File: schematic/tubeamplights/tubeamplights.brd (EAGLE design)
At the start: 68.8 x 53 mm, 6 parts

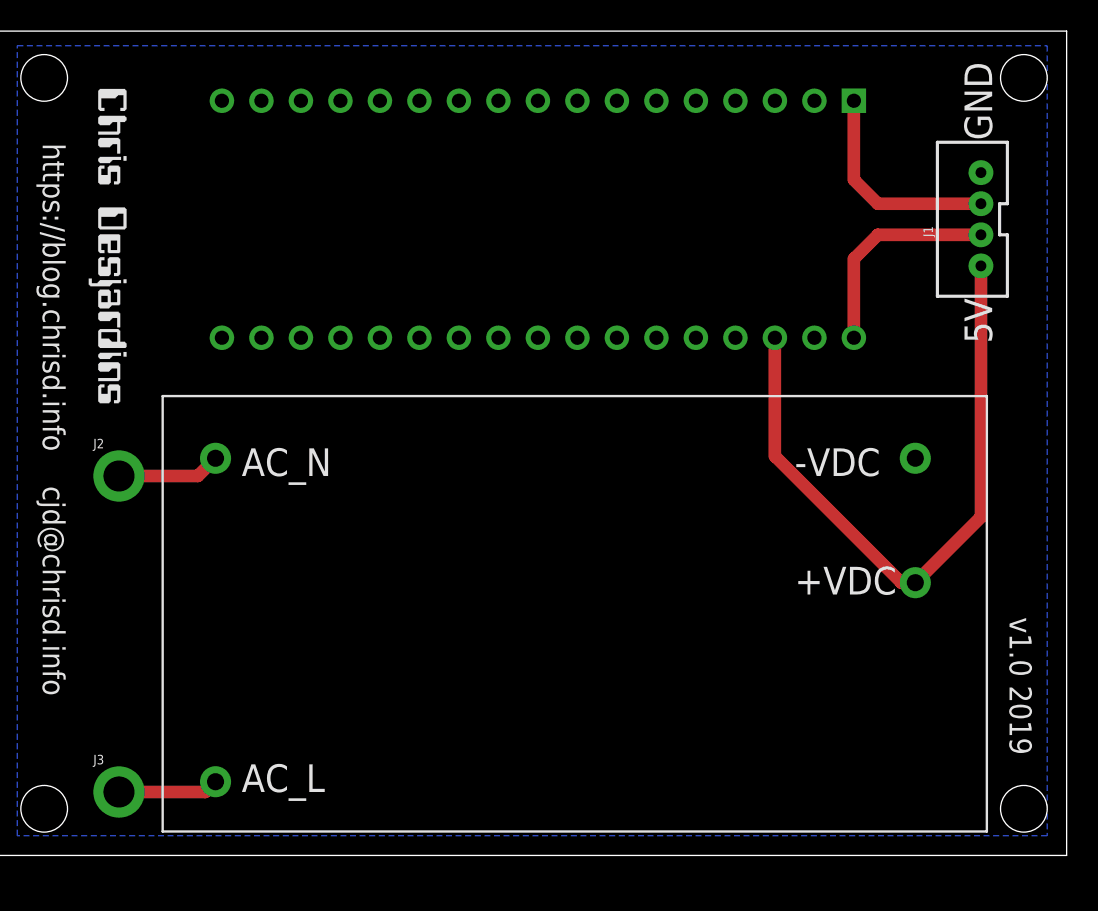
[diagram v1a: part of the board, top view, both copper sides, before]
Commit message: Fix the reg footprint
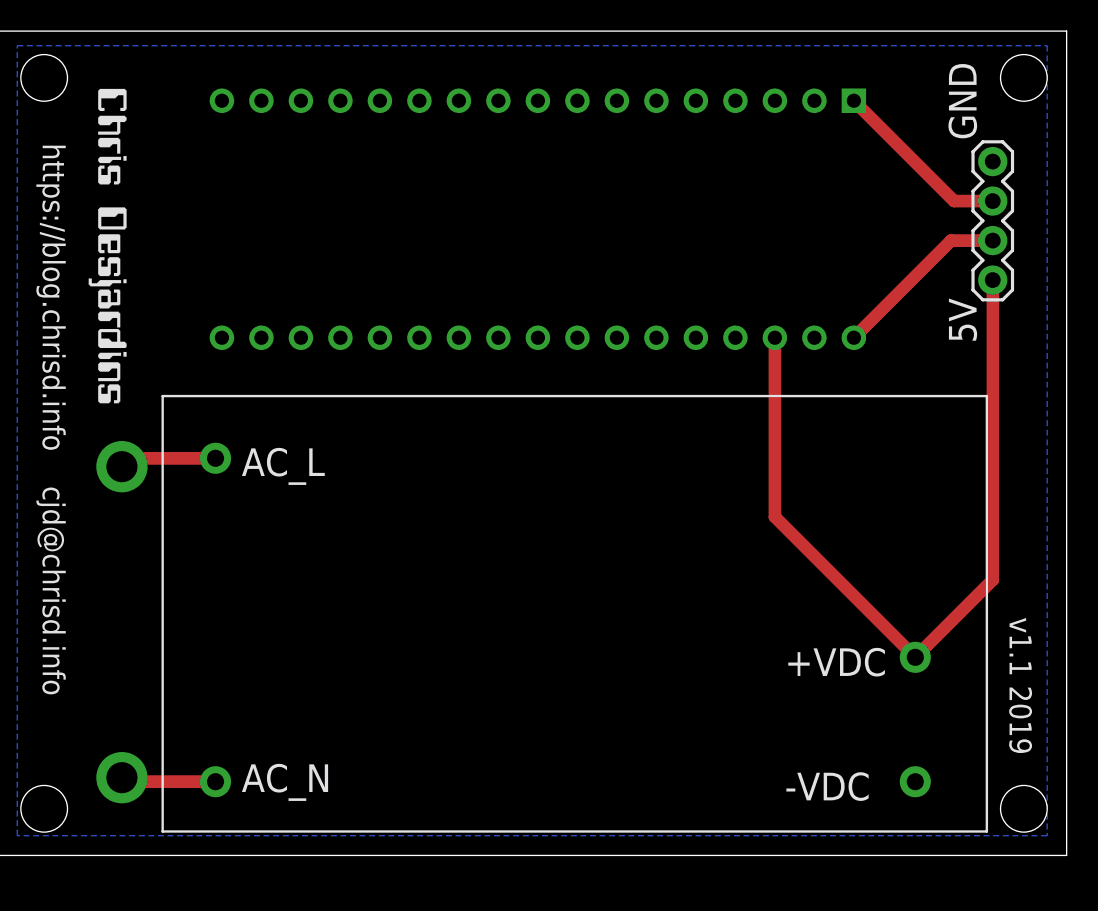
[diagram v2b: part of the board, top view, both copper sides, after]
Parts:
- removed J1: (no value), SparkFun-Connectors:JST-4-PTH-VERT
- added J4: (no value), SparkFun-Connectors:1X04
- moved J3 20.9 mm to (8.00, 25.0)
- moved J2 19.4 mm to (8.00, 5.00)
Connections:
- net GND: now also J4.4; no longer J1.4
- net MOSI: now also J4.3; no longer J1.3
- net SCK: now also J4.2; no longer J1.2
- net VIN: now also J4.1; no longer J1.1
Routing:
- net VIN: track 42.1 -> 50.6 mm
- net SCK: track 13.9 -> 11.5 mm
- net MOSI: track 13.9 -> 11.6 mm
- net AC_N: track 6.68 -> 6.13 mm
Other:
- board text added: "v1.1 2019"
- board text removed: "v1.0 2019"
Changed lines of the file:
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@@
 <wire x1="0" y1="53.01" x2="0" y2="0" width="0" layer="20"/>
 <text x="2.905" y="45.8" size="1.4224" layer="21" font="vector" rot="SR270">https://blog.chrisd.info    cjd@chrisd.info</text>
-<text x="63.96" y="35.83" size="1.778" layer="21" rot="R90" align="bottom-right">5V</text>
-<text x="63.96" y="45.99" size="1.778" layer="21" rot="R90">GND</text>
-<text x="65.08" y="15.32" size="1.4224" layer="21" font="vector" rot="SR270">v1.0 2019</text>
+<text x="62.96" y="35.83" size="1.778" layer="21" rot="R90" align="bottom-right">5V</text>
+<text x="62.96" y="45.99" size="1.778" layer="21" rot="R90">GND</text>
+<text x="65.08" y="15.32" size="1.4224" layer="21" font="vector" rot="SR270">v1.1 2019</text>
 <hole x="66" y="3" drill="3"/>
 <hole x="66" y="50" drill="3"/>
@@
 </autorouter>
 <elements>
-<element name="J1" library="SparkFun-Connectors" library_urn="urn:adsk.eagle:library:513" package="JST-4-PTH-VERT" package3d_urn="urn:adsk.eagle:package:38102/1" value="" x="62.69" y="40.91" smashed="yes" rot="R90">
-<attribute name="NAME" x="60.15" y="39.767" size="0.6096" layer="25" font="vector" ratio="20" rot="R90"/>
-<attribute name="PROD_ID" value="CONN-13251" x="143.97" y="58.69" size="1.778" layer="27" rot="R90" display="off"/>
-<attribute name="VALUE" x="65.992" y="39.259" size="0.6096" layer="27" font="vector" ratio="20" rot="R90"/>
+<element name="J2" library="SparkFun-Connectors" library_urn="urn:adsk.eagle:library:513" package="1X01_2MM" package3d_urn="urn:adsk.eagle:package:38029/1" value="" x="8" y="5" smashed="yes">
+<attribute name="VALUE" x="6.349" y="2.587" size="0.6096" layer="27" font="vector" ratio="20"/>
 </element>
-<element name="J2" library="SparkFun-Connectors" library_urn="urn:adsk.eagle:library:513" package="1X01_2MM" package3d_urn="urn:adsk.eagle:package:38029/1" value="" x="7.81" y="24.4" smashed="yes">
-<attribute name="NAME" x="6.159" y="26.178" size="0.6096" layer="25" font="vector" ratio="20"/>
-<attribute name="VALUE" x="6.159" y="21.987" size="0.6096" layer="27" font="vector" ratio="20"/>
-</element>
-<element name="J3" library="SparkFun-Connectors" library_urn="urn:adsk.eagle:library:513" package="1X01_2MM" package3d_urn="urn:adsk.eagle:package:38029/1" value="" x="7.81" y="4.08" smashed="yes">
-<attribute name="NAME" x="6.159" y="5.858" size="0.6096" layer="25" font="vector" ratio="20"/>
-<attribute name="VALUE" x="6.159" y="1.667" size="0.6096" layer="27" font="vector" ratio="20"/>
+<element name="J3" library="SparkFun-Connectors" library_urn="urn:adsk.eagle:library:513" package="1X01_2MM" package3d_urn="urn:adsk.eagle:package:38029/1" value="" x="8" y="25" smashed="yes">
+<attribute name="VALUE" x="6.349" y="22.587" size="0.6096" layer="27" font="vector" ratio="20"/>
 </element>
 <element name="U$1" library="ChrisD" package="ARDUINO_PRO_MICRO" value="ARDUINO_PRO_MICRO" x="10.62" y="49.8" smashed="yes" rot="R270"/>
 <element name="U$2" library="meanwell-mpm-20-x" package="MPM-20-X" value="MPM-20-X" x="10.62" y="1.54" smashed="yes"/>
 <element name="U$3" library="desjardins" package="LOGO" value="" x="6.4725" y="49.37" smashed="yes" rot="R270"/>
+<element name="J4" library="SparkFun-Connectors" library_urn="urn:adsk.eagle:library:513" package="1X04" package3d_urn="urn:adsk.eagle:package:38085/1" value="" x="64" y="37" smashed="yes" rot="R90">
+<attribute name="PROD_ID" value="CONN-09696" x="64" y="37" size="1.778" layer="27" rot="R90" display="off"/>
+<attribute name="VALUE" x="66.032" y="35.73" size="0.6096" layer="27" font="vector" ratio="20" rot="R90"/>
+</element>
 </elements>
 <signals>
@@
 <contactref element="U$2" pad="+VDC"/>
 <contactref element="U$1" pad="P32"/>
-<contactref element="J1" pad="1"/>
-<wire x1="59.02" y1="17.54" x2="58.12" y2="17.54" width="0.8128" layer="1"/>
-<wire x1="58.12" y1="17.54" x2="49.99" y2="25.67" width="0.8128" layer="1"/>
-<wire x1="49.99" y1="25.67" x2="49.99" y2="33.29" width="0.8128" layer="1"/>
-<wire x1="63.24" y1="37.91" x2="63.24" y2="21.76" width="0.8128" layer="1"/>
-<wire x1="63.24" y1="21.76" x2="59.02" y2="17.54" width="0.8128" layer="1"/>
+<contactref element="J4" pad="1"/>
+<wire x1="64" y1="37" x2="64" y2="17.72" width="0.8128" layer="1"/>
+<wire x1="64" y1="17.72" x2="59.02" y2="12.74" width="0.8128" layer="1"/>
+<wire x1="49.99" y1="33.29" x2="49.99" y2="21.77" width="0.8128" layer="1"/>
+<wire x1="49.99" y1="21.77" x2="59.02" y2="12.74" width="0.8128" layer="1"/>
 </signal>
 <signal name="GND">
@@
 <contactref element="U$1" pad="P31"/>
 <contactref element="U$1" pad="P6"/>
-<contactref element="J1" pad="4"/>
 <polygon width="0.1524" layer="16">
 <vertex x="1.27" y="1.27"/>
@@
 <vertex x="67.5" y="1.27"/>
 </polygon>
+<contactref element="J4" pad="4"/>
 </signal>
 <signal name="AC_N">
 <contactref element="U$2" pad="AC_N"/>
 <contactref element="J2" pad="1"/>
-<wire x1="14.02" y1="25.54" x2="12.88" y2="24.4" width="0.8128" layer="1"/>
-<wire x1="12.88" y1="24.4" x2="7.81" y2="24.4" width="0.8128" layer="1"/>
+<wire x1="14.02" y1="4.74" x2="8.26" y2="4.74" width="0.8128" layer="1"/>
+<wire x1="8.26" y1="4.74" x2="8" y2="5" width="0.8128" layer="1"/>
 </signal>
 <signal name="AC_L">
 <contactref element="U$2" pad="AC_L"/>
 <contactref element="J3" pad="1"/>
-<wire x1="14.02" y1="4.74" x2="13.36" y2="4.08" width="0.8128" layer="1"/>
-<wire x1="13.36" y1="4.08" x2="7.81" y2="4.08" width="0.8128" layer="1"/>
+<wire x1="8" y1="25" x2="8.54" y2="25.54" width="0.8128" layer="1"/>
+<wire x1="8.54" y1="25.54" x2="14.02" y2="25.54" width="0.8128" layer="1"/>
 </signal>
 <signal name="SCK">
 <contactref element="U$1" pad="P34"/>
-<contactref element="J1" pad="2"/>
-<wire x1="63.24" y1="39.91" x2="56.61" y2="39.91" width="0.8128" layer="1"/>
-<wire x1="56.61" y1="39.91" x2="55.07" y2="38.37" width="0.8128" layer="1"/>
-<wire x1="55.07" y1="38.37" x2="55.07" y2="33.29" width="0.8128" layer="1"/>
+<contactref element="J4" pad="2"/>
+<wire x1="55.07" y1="33.29" x2="61.32" y2="39.54" width="0.8128" layer="1"/>
+<wire x1="61.32" y1="39.54" x2="64" y2="39.54" width="0.8128" layer="1"/>
 </signal>
 <signal name="MOSI">
 <contactref element="U$1" pad="P1"/>
-<contactref element="J1" pad="3"/>
-<wire x1="63.24" y1="41.91" x2="56.61" y2="41.91" width="0.8128" layer="1"/>
-<wire x1="56.61" y1="41.91" x2="55.07" y2="43.45" width="0.8128" layer="1"/>
-<wire x1="55.07" y1="43.45" x2="55.07" y2="48.53" width="0.8128" layer="1"/>
+<contactref element="J4" pad="3"/>
+<wire x1="55.07" y1="48.53" x2="61.52" y2="42.08" width="0.8128" layer="1"/>
+<wire x1="61.52" y1="42.08" x2="64" y2="42.08" width="0.8128" layer="1"/>
 </signal>
 </signals>
